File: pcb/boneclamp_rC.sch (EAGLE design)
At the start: 133 parts, among them U1 OPA365AIDBVR, U10 AD5686, U11 LM2663, U12 MAX1735, U13 TLV70245, U14 REF5040MDREP, U15 AD8032ARZ-REEL7, U16 24C, U2 OPA365AIDBVR, U3 OPA365AIDBVR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

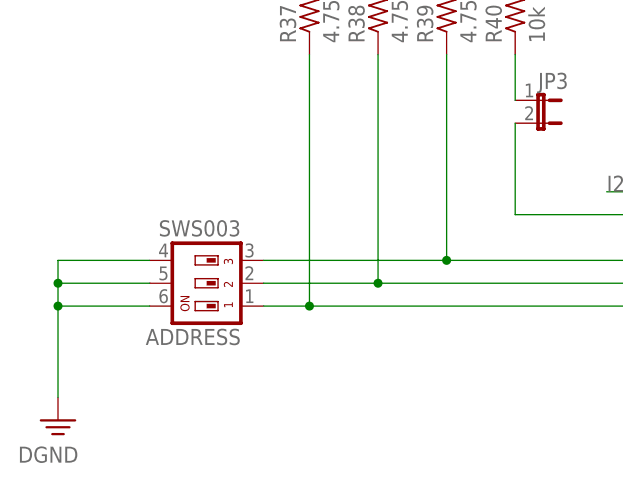
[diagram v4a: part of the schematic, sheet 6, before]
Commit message: Started EEPROM circuit.
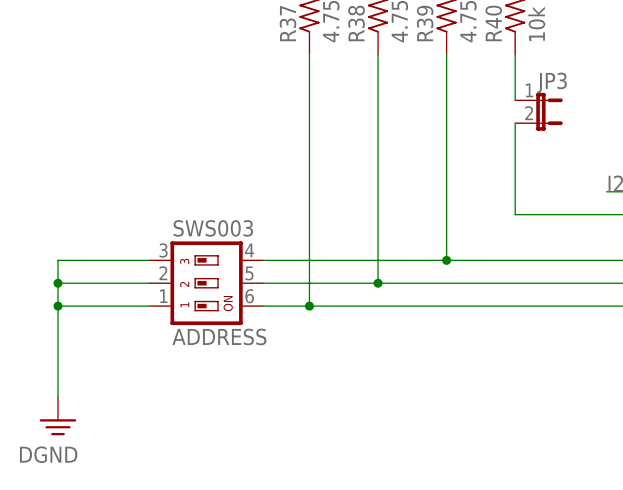
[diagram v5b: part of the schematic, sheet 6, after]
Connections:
- net DGND: now also ADDRESS.1, ADDRESS.2, ADDRESS.3; no longer ADDRESS.4, ADDRESS.5, ADDRESS.6
- net N$14: now also ADDRESS.6; no longer ADDRESS.1
- net N$18: now also ADDRESS.5; no longer ADDRESS.2
- net N$19: now also ADDRESS.4; no longer ADDRESS.3
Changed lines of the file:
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@@
 <instance part="VDRIVE" gate="G$1" x="-81.28" y="63.5"/>
 <instance part="JP3" gate="A" x="-48.26" y="40.64" rot="R270"/>
-<instance part="ADDRESS" gate="G$1" x="-83.82" y="20.32" rot="R90"/>
+<instance part="ADDRESS" gate="G$1" x="-86.36" y="20.32" rot="MR90"/>
 <instance part="I2C2_SDA" gate="G$1" x="15.24" y="25.4"/>
 <instance part="DGND6" gate="PE" x="50.8" y="5.08"/>
@@
 <net name="DGND" class="0">
 <segment>
+<wire x1="-101.6" y1="22.86" x2="-101.6" y2="20.32" width="0.1524" layer="91"/>
+<pinref part="DGND8" gate="PE" pin="PE"/>
+<pinref part="ADDRESS" gate="G$1" pin="3"/>
+<wire x1="-101.6" y1="20.32" x2="-101.6" y2="17.78" width="0.1524" layer="91"/>
+<wire x1="-101.6" y1="17.78" x2="-101.6" y2="7.62" width="0.1524" layer="91"/>
+<wire x1="-101.6" y1="22.86" x2="-91.44" y2="22.86" width="0.1524" layer="91"/>
+<pinref part="ADDRESS" gate="G$1" pin="2"/>
 <wire x1="-91.44" y1="20.32" x2="-101.6" y2="20.32" width="0.1524" layer="91"/>
-<wire x1="-101.6" y1="20.32" x2="-101.6" y2="17.78" width="0.1524" layer="91"/>
+<junction x="-101.6" y="20.32"/>
+<pinref part="ADDRESS" gate="G$1" pin="1"/>
 <wire x1="-101.6" y1="17.78" x2="-91.44" y2="17.78" width="0.1524" layer="91"/>
-<wire x1="-101.6" y1="17.78" x2="-101.6" y2="7.62" width="0.1524" layer="91"/>
 <junction x="-101.6" y="17.78"/>
-<pinref part="DGND8" gate="PE" pin="PE"/>
-<pinref part="ADDRESS" gate="G$1" pin="5"/>
-<pinref part="ADDRESS" gate="G$1" pin="6"/>
-<wire x1="-101.6" y1="20.32" x2="-101.6" y2="22.86" width="0.1524" layer="91"/>
-<junction x="-101.6" y="20.32"/>
-<pinref part="ADDRESS" gate="G$1" pin="4"/>
-<wire x1="-101.6" y1="22.86" x2="-91.44" y2="22.86" width="0.1524" layer="91"/>
 </segment>
 <segment>
@@
 <segment>
 <pinref part="U16" gate="G$1" pin="A0"/>
-<wire x1="-78.74" y1="17.78" x2="-73.66" y2="17.78" width="0.1524" layer="91"/>
 <wire x1="-73.66" y1="17.78" x2="-15.24" y2="17.78" width="0.1524" layer="91"/>
 <wire x1="-73.66" y1="17.78" x2="-73.66" y2="45.72" width="0.1524" layer="91"/>
+<pinref part="R37" gate="G$1" pin="1"/>
+<pinref part="ADDRESS" gate="G$1" pin="6"/>
+<wire x1="-78.74" y1="17.78" x2="-73.66" y2="17.78" width="0.1524" layer="91"/>
 <junction x="-73.66" y="17.78"/>
-<pinref part="R37" gate="G$1" pin="1"/>
-<pinref part="ADDRESS" gate="G$1" pin="1"/>
 </segment>
 </net>
@@
 <pinref part="U16" gate="G$1" pin="A1"/>
 <wire x1="-15.24" y1="20.32" x2="-66.04" y2="20.32" width="0.1524" layer="91"/>
-<pinref part="ADDRESS" gate="G$1" pin="2"/>
 <pinref part="R38" gate="G$1" pin="1"/>
-<wire x1="-66.04" y1="20.32" x2="-78.74" y2="20.32" width="0.1524" layer="91"/>
 <wire x1="-66.04" y1="45.72" x2="-66.04" y2="20.32" width="0.1524" layer="91"/>
+<pinref part="ADDRESS" gate="G$1" pin="5"/>
+<wire x1="-78.74" y1="20.32" x2="-66.04" y2="20.32" width="0.1524" layer="91"/>
 <junction x="-66.04" y="20.32"/>
 </segment>
@@
 <wire x1="-58.42" y1="22.86" x2="-58.42" y2="45.72" width="0.1524" layer="91"/>
 <pinref part="R39" gate="G$1" pin="1"/>
-<pinref part="ADDRESS" gate="G$1" pin="3"/>
+<pinref part="ADDRESS" gate="G$1" pin="4"/>
 <wire x1="-78.74" y1="22.86" x2="-58.42" y2="22.86" width="0.1524" layer="91"/>
 <junction x="-58.42" y="22.86"/>

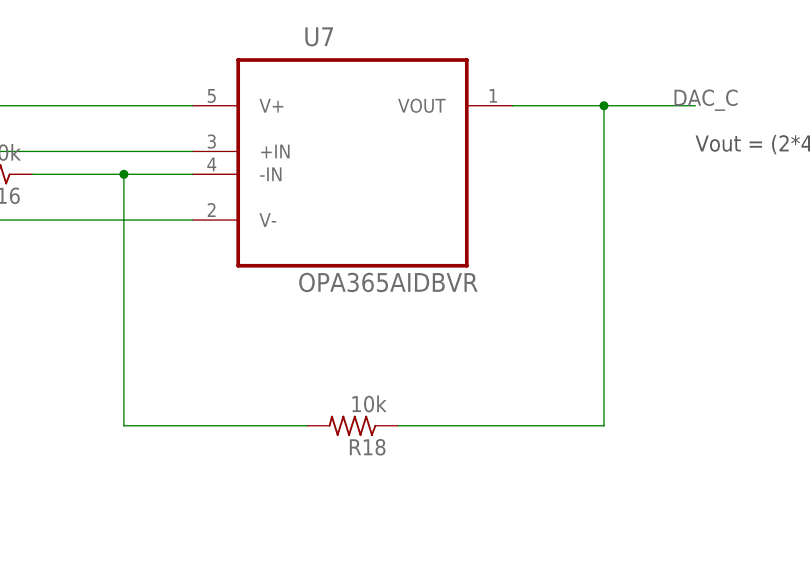
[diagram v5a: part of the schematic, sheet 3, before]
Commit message: Started laying out the AO buffer stage.
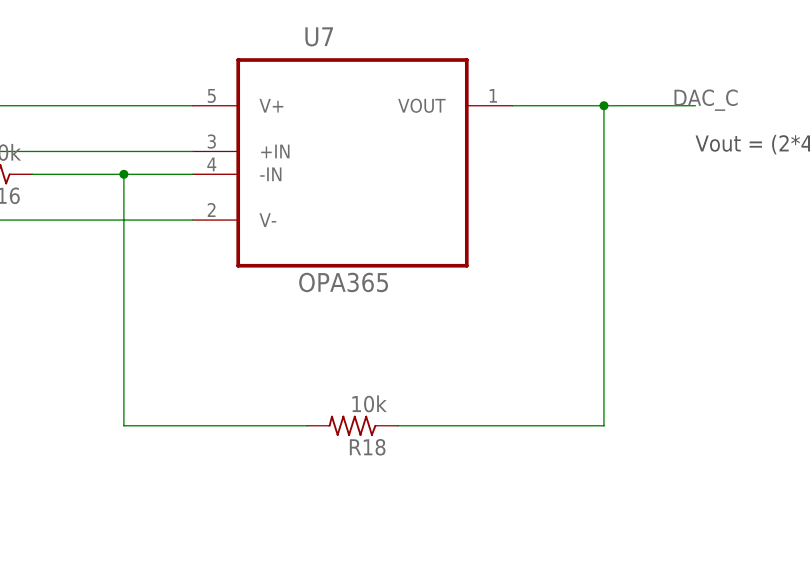
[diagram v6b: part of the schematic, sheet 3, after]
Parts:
- U7: value OPA365AIDBVR -> OPA365
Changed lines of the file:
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@@
 <part name="C16" library="rcl" deviceset="C-EU" device="C0603" value="0.1uF"/>
 <part name="SUPPLY31" library="supply2" deviceset="AGND" device=""/>
-<part name="U7" library="ti-extended" deviceset="OPA365AIDBVR" device=""/>
+<part name="U7" library="ti-extended" deviceset="OPA365AIDBVR" device="" value="OPA365"/>
 <part name="R16" library="rcl" deviceset="R-US_" device="R0603" value="10k"/>
 <part name="R18" library="rcl" deviceset="R-US_" device="R0603" value="10k"/>

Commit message: Finished basic DAC buffer layout.
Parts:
- renumbered JP3 to ~W
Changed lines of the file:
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@@
 <part name="SUPPLY10" library="supply2" deviceset="AGND" device=""/>
 <part name="SUPPLY2" library="supply2" deviceset="AGND" device=""/>
-<part name="JP3" library="jumper" deviceset="JP1E" device=""/>
+<part name="~W" library="jumper" deviceset="JP1E" device=""/>
 <part name="ADDRESS" library="smd-special" deviceset="SWS003" device=""/>
 <part name="I2C2_SDA" library="testpad" deviceset="TP" device="B1,27"/>
@@
 <instance part="I2C2_SCLK" gate="G$1" x="-25.4" y="33.02"/>
 <instance part="VDRIVE" gate="G$1" x="-81.28" y="63.5"/>
-<instance part="JP3" gate="A" x="-48.26" y="40.64" rot="R270"/>
+<instance part="~W" gate="A" x="-48.26" y="40.64" rot="R270"/>
 <instance part="ADDRESS" gate="G$1" x="-86.36" y="20.32" rot="MR90"/>
 <instance part="I2C2_SDA" gate="G$1" x="15.24" y="25.4"/>
@@
 <segment>
 <pinref part="R40" gate="G$1" pin="1"/>
-<pinref part="JP3" gate="A" pin="1"/>
+<pinref part="~W" gate="A" pin="1"/>
 <wire x1="-50.8" y1="40.64" x2="-50.8" y2="45.72" width="0.1524" layer="91"/>
 </segment>
@@
 <pinref part="U16" gate="G$1" pin="WP"/>
 <wire x1="-50.8" y1="27.94" x2="-15.24" y2="27.94" width="0.1524" layer="91"/>
-<pinref part="JP3" gate="A" pin="2"/>
+<pinref part="~W" gate="A" pin="2"/>
 <wire x1="-50.8" y1="27.94" x2="-50.8" y2="38.1" width="0.1524" layer="91"/>
 </segment>

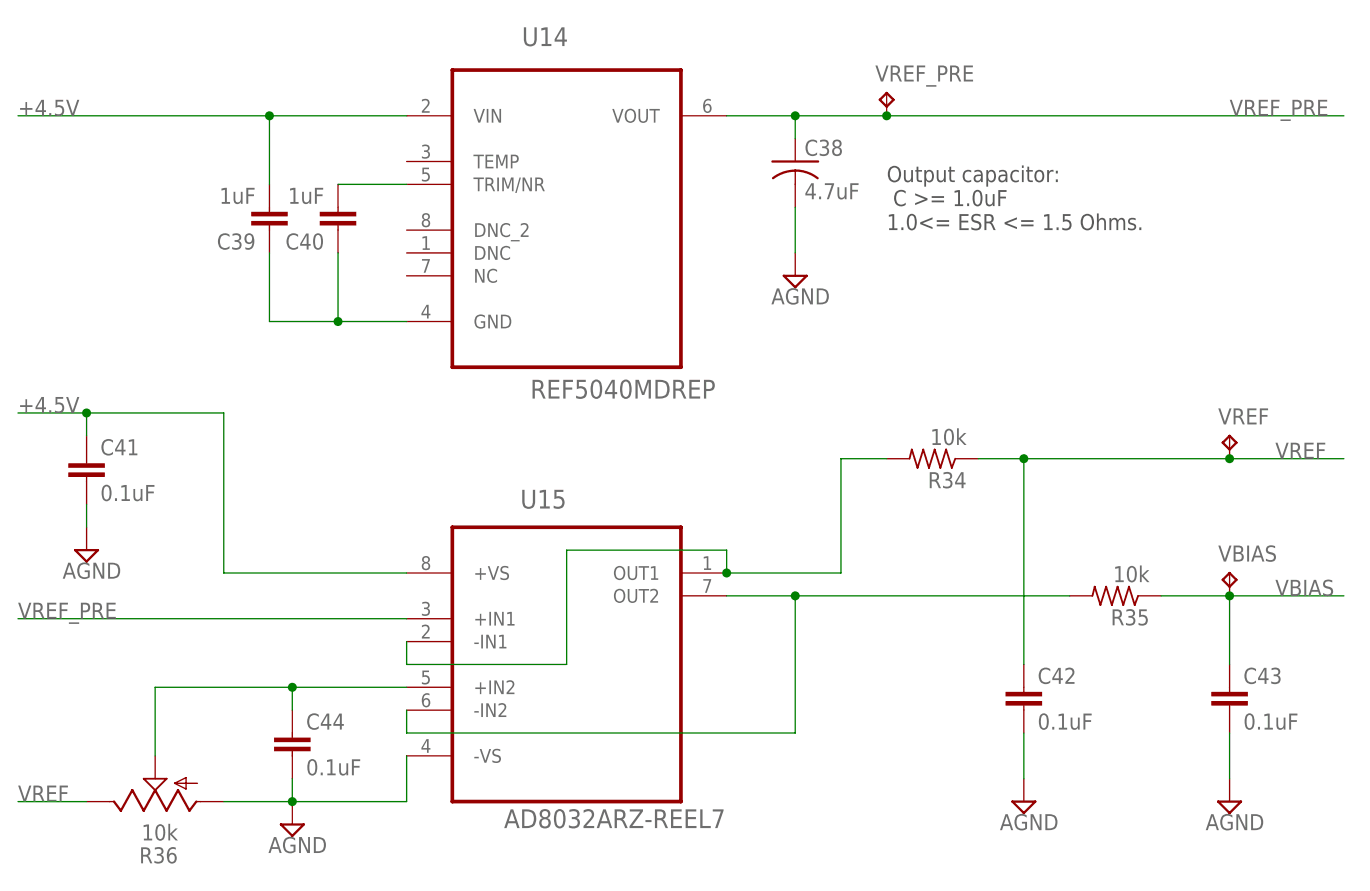
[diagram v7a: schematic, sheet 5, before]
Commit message: Analog buffering stage is pretty much finished. Next will be the regulated power circuitry, then comes the mixed signal ICs.
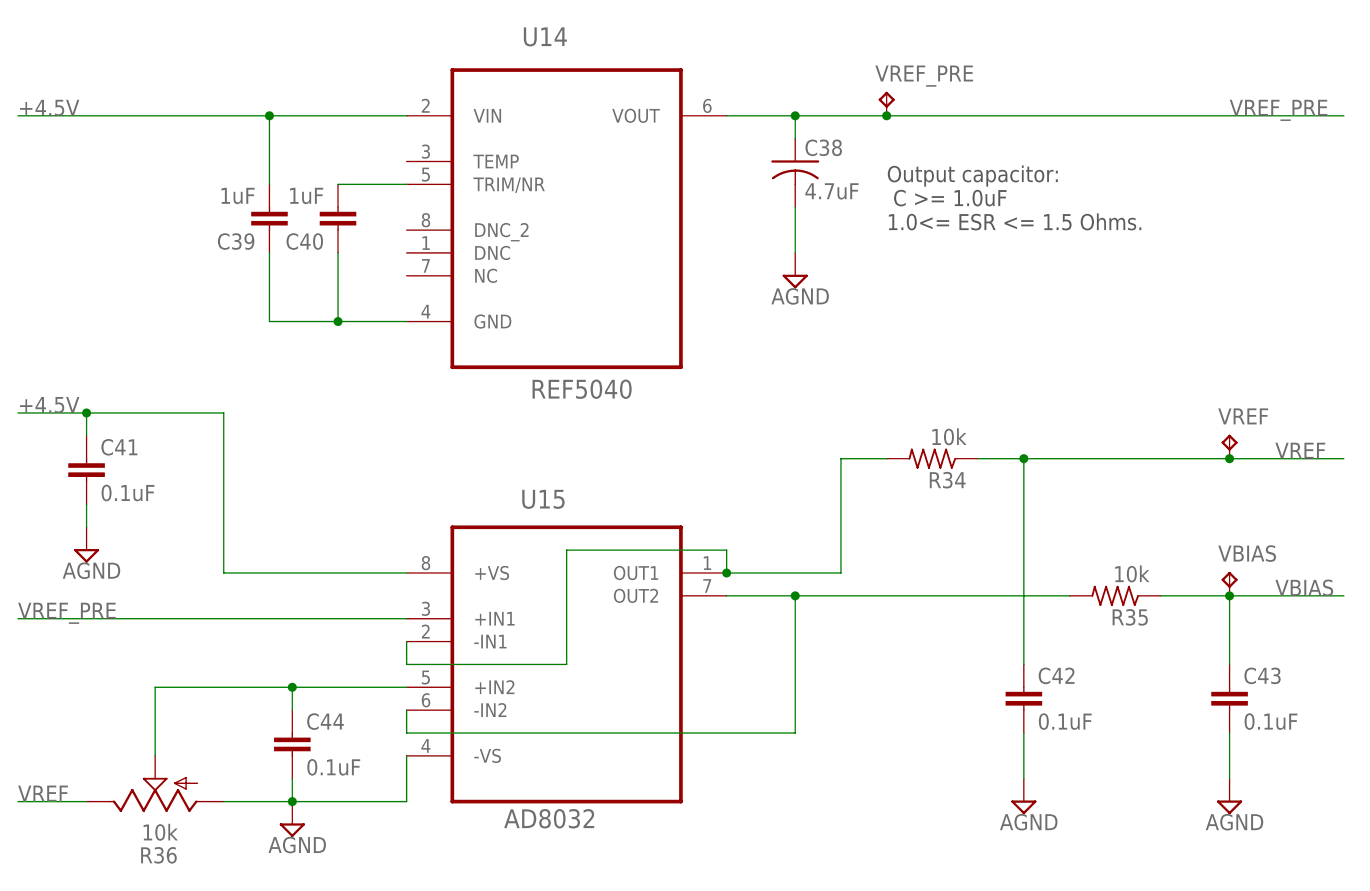
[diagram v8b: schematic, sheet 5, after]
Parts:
- U14: value REF5040MDREP -> REF5040
- U15: value AD8032ARZ-REEL7 -> AD8032
- U5: value ADS8331IBPW -> ADS8331
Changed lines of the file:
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@@
 <part name="R24" library="rcl" deviceset="R-US_" device="R0603" value="10k"/>
 <part name="R25" library="rcl" deviceset="R-US_" device="R0603" value="10k"/>
-<part name="U5" library="ti-extended" deviceset="ADS8331IBPW" device=""/>
+<part name="U5" library="ti-extended" deviceset="ADS8331IBPW" device="" value="ADS8331"/>
 <part name="U1" library="ti-extended" deviceset="OPA365AIDBVR" device=""/>
 <part name="R1" library="rcl" deviceset="R-US_" device="R0603" value="20k"/>
 <part name="R3" library="rcl" deviceset="R-US_" device="R0603" value="10k"/>
-<part name="U14" library="ti-extended" deviceset="REF5040MDREP" device=""/>
+<part name="U14" library="ti-extended" deviceset="REF5040MDREP" device="" value="REF5040"/>
 <part name="C39" library="rcl" deviceset="C-EU" device="C0603" value="1uF"/>
 <part name="C40" library="rcl" deviceset="C-EU" device="C0603" value="1uF"/>
@@
 <part name="C7" library="rcl" deviceset="C-EU" device="C0603" value="0.1uF"/>
 <part name="SUPPLY36" library="supply2" deviceset="AGND" device=""/>
-<part name="U15" library="analog-devices-02" deviceset="AD8032ARZ-REEL7" device=""/>
+<part name="U15" library="analog-devices-02" deviceset="AD8032ARZ-REEL7" device="" value="AD8032"/>
 <part name="C44" library="rcl" deviceset="C-EU" device="C0603" value="0.1uF"/>
 <part name="C41" library="rcl" deviceset="C-EU" device="C0603" value="0.1uF"/>
